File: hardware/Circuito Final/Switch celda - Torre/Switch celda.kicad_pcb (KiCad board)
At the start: 2 copper layers, 93.8 x 40 mm, 28 parts, among them Q1 MMBT2222A, Q2 MMBT2907A, Q3 MMBT2222A

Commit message: Subida de la versión torrecita
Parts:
- added TPgnd1: TP_gnd, Connector_PinHeader_2.54mm:PinHeader_1x01_P2.54mm_Vertical, F.Cu at (158.0, 111.2)
- added TPgnd2: TP_gnd, Connector_PinHeader_2.54mm:PinHeader_1x01_P2.54mm_Vertical, F.Cu at (151.0, 116.8)
- J_In_Out_1: value Conn_01x05_Socket -> Conn_01x06_Socket; footprint Connector_PinSocket_2.54mm:PinSocket_1x05_P2.54mm_Vertical -> Connector_PinSocket_2.54mm:PinSocket_1x06_P2.54mm_Vertical
- moved TP3 6.01 mm to (170.5, 115.5)
- moved TP1 4.75 mm to (165.8, 115.8)
- moved J_In_Out_1 2.54 mm to (103.5, 108.2)
- moved TP2 2.50 mm to (160.8, 115.8)
- moved Jumper_cell_neg_1 1.79 mm to (176.8, 116.8)
- moved Q3 0.59 mm to (151.2, 99.8), turned to 0 degrees
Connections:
- J_In_Out_1 pad 4: Vcc -> 0
- J_In_Out_1 pad 5: bus_pos -> Vcc
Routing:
- net Net-(Q2-B): track 37.5 -> 132.6 mm, vias 1 -> 0
- net Net-(Qinv1-D): track 53.3 -> 128.5 mm, vias 1 -> 0
- net bus_pos: track 14.9 -> 74.4 mm
- net 0: track 0.00 -> 9.42 mm
- net Net-(Q3-B): track 9.46 -> 4.79 mm
- net Net-(S1-G): track 155.5 -> 159.1 mm
- net Net-(Q3-C): track 10.0 -> 6.56 mm
- net Vcell_neg: track 108.8 -> 112.3 mm
- net bus_neg: track 65.6 -> 63.0 mm
- net cell_neg1: track 28.3 -> 26.5 mm
- net cell_neg4: track 17.6 -> 15.8 mm
- net cell_neg2: track 24.7 -> 23.0 mm
- net cell_neg6: track 10.4 -> 8.59 mm
- net cell_neg5: track 14.1 -> 12.3 mm
- net cell_neg3: track 21.2 -> 19.4 mm
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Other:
- board size 93.8 x 40 mm -> 97 x 40 mm

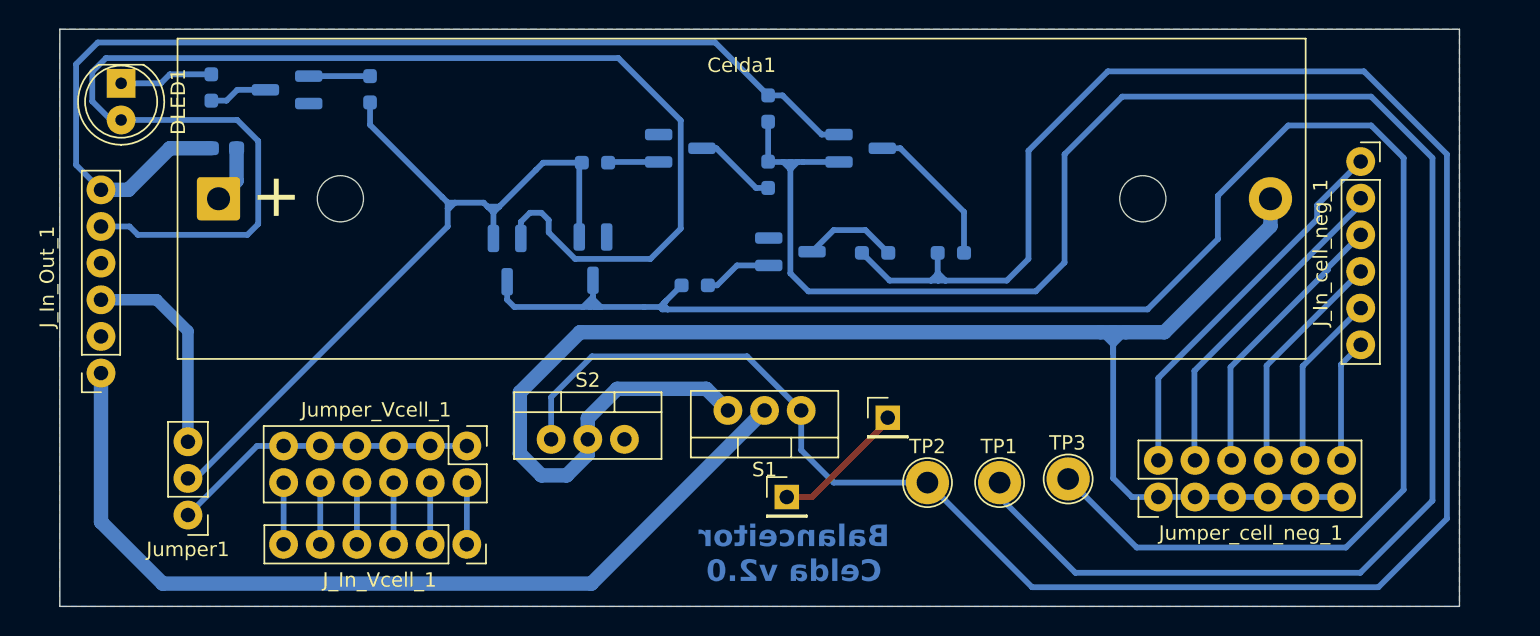
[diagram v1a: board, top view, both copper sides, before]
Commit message: Se duplican dos de las 3 tiras de pines del circuito de celda topología torre
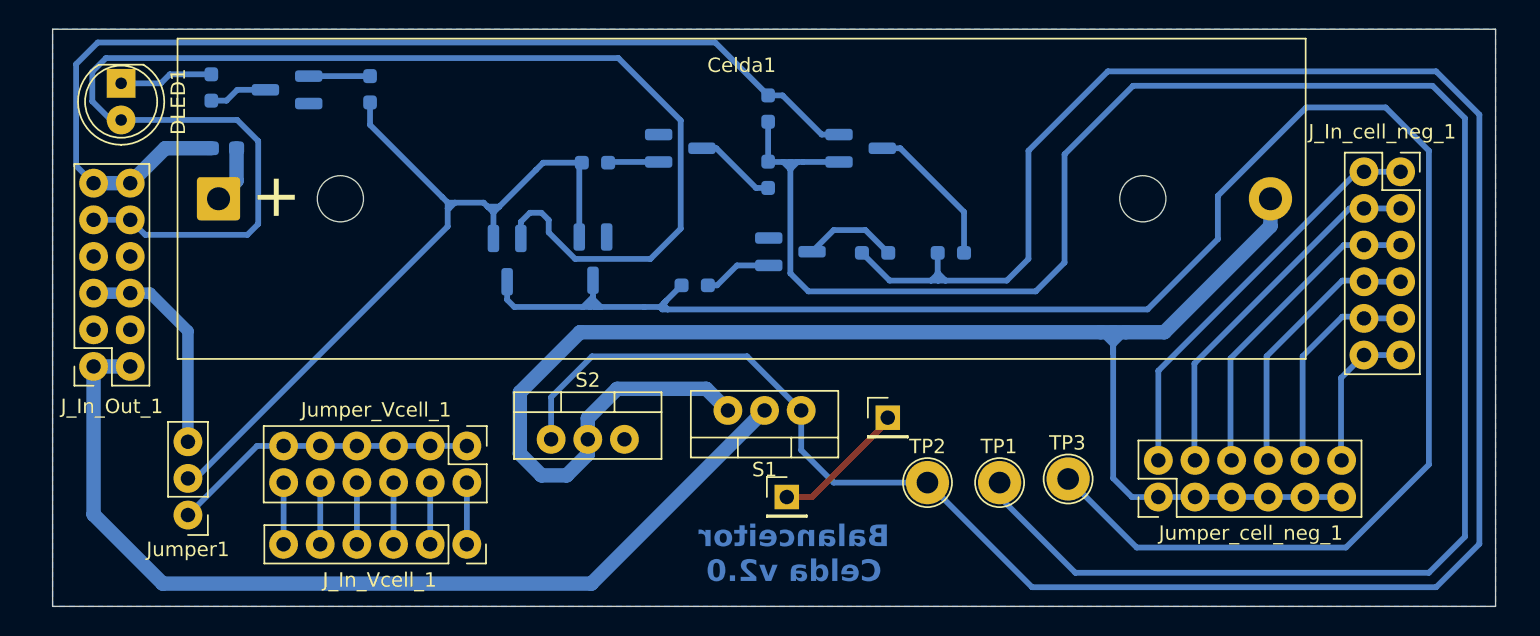
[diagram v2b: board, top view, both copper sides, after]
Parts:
- J_In_Out_1, J_In_cell_neg_1: value Conn_01x06_Socket -> Conn_02x06_Odd_Even; footprint Connector_PinSocket_2.54mm:PinSocket_1x06_P2.54mm_Vertical -> Connector_PinSocket_2.54mm:PinSocket_2x06_P2.54mm_Vertical
- moved J_In_cell_neg_1 2.85 mm to (193.5, 94.2)
- moved J_In_Out_1 0.69 mm to (103.0, 107.7)
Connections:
- J_In_Out_1 pad 2: 0 -> bus_neg
- J_In_Out_1 pad 3: Vcell_banco -> 0
- J_In_Out_1 pad 5: Vcc -> Vcell_banco
- J_In_Out_1 pad 6: bus_pos -> Vcell_banco
- J_In_cell_neg_1 pad 2: cell_neg2 -> cell_neg1
- J_In_cell_neg_1 pad 3: cell_neg3 -> cell_neg2
- J_In_cell_neg_1 pad 4: cell_neg4 -> cell_neg2
- J_In_cell_neg_1 pad 5: cell_neg5 -> cell_neg3
- J_In_cell_neg_1 pad 6: cell_neg6 -> cell_neg3
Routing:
- net Net-(Q2-B): track 132.6 -> 140.8 mm
- net Net-(S1-G): track 159.1 -> 166.3 mm
- net Net-(Qinv1-D): track 128.5 -> 132.3 mm
- net bus_neg: track 63.0 -> 66.3 mm
- net cell_neg5: track 12.3 -> 15.3 mm
- net cell_neg4: track 15.8 -> 18.8 mm
- net cell_neg3: track 19.4 -> 22.1 mm
- net cell_neg2: track 23.0 -> 25.5 mm
- net cell_neg1: track 26.5 -> 28.7 mm
- net cell_neg6: track 8.59 -> 10.5 mm
- net Vcc: track 97.5 -> 98.2 mm
- net Vcell_banco: track 14.6 -> 15.3 mm
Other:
- board size 97 x 40 mm -> 100 x 40 mm

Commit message: Cambios al circuito de la celda en modo torre: clearance de 0.5mm (en lugar de la mínima), buses de potencia de 1.5mm (en lugar de 1mm) y resistores SMD de tamaño 1206 (en lugar de 0603)
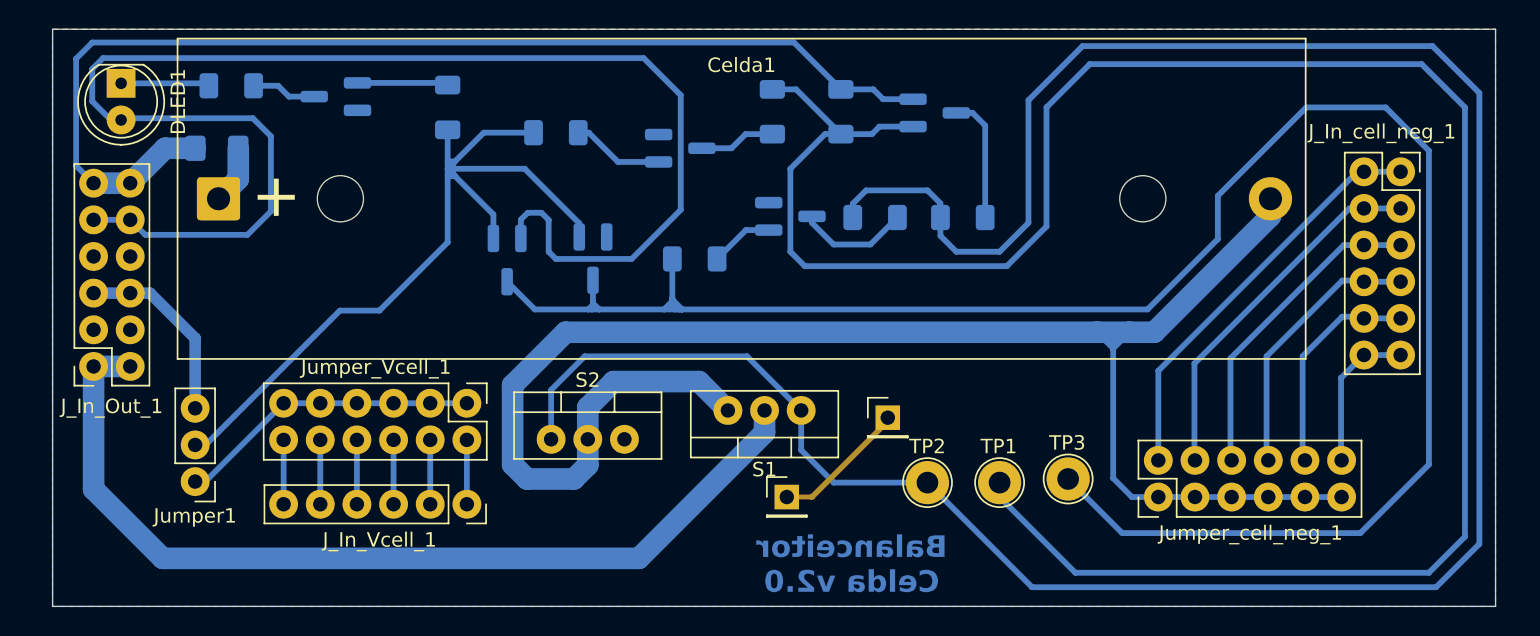
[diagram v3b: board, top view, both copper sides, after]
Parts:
- F1: footprint Fuse:Fuse_0603_1608Metric_Pad1.05x0.95mm_HandSolder -> Fuse:Fuse_1206_3216Metric_Pad1.42x1.75mm_HandSolder
- R1, R2, R3, R4, R5, R6, RLED1, RLED2: footprint Resistor_SMD:R_0603_1608Metric_Pad0.98x0.95mm_HandSolder -> Resistor_SMD:R_1206_3216Metric_Pad1.30x1.75mm_HandSolder
- moved Q2 5.69 mm to (161.2, 90.1)
- moved RLED1 5.53 mm to (127.5, 89.8)
- moved R2 5.05 mm to (154.8, 90.0)
- moved R3 4.38 mm to (150.0, 90.0)
- moved R1 3.41 mm to (135.0, 91.5)
- moved QLED1 3.41 mm to (119.8, 89.0)
- moved Jumper_Vcell_1 2.96 mm to (128.8, 110.2)
- moved J_In_Vcell_1 2.78 mm to (128.8, 117.2)
- moved R4 2.59 mm to (163.2, 97.4)
- moved Q3 2.45 mm to (151.2, 97.3)
- moved R5 2.45 mm to (157.1, 97.4)
- moved Jumper1 2.37 mm to (110.0, 115.7)
- moved R6 1.83 mm to (144.6, 100.2)
- moved RLED2 1.38 mm to (112.5, 88.2), turned to 180 degrees
- moved F1 0.50 mm to (111.5, 92.6)
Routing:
- net Net-(Q2-B): track 140.8 -> 146.7 mm
- net Vcell_neg: track 112.3 -> 116.0 mm
- net bus_pos: track 74.0 -> 77.7 mm
- net Net-(S1-G): track 166.3 -> 169.5 mm
- net Vin: track 55.6 -> 58.7 mm
- net Net-(Q1-B): track 3.52 -> 6.41 mm
- net Vcc: track 98.2 -> 101.0 mm
- net Vcell_banco: track 15.3 -> 13.2 mm
- net Net-(QLED1-B): track 4.25 -> 6.31 mm
- net Net-(Q2-C): track 10.3 -> 8.74 mm
- net bus_neg: track 66.3 -> 64.7 mm
- net Net-(Q3-C): track 6.56 -> 7.77 mm
- net Net-(Qinv1-D): track 132.3 -> 133.3 mm

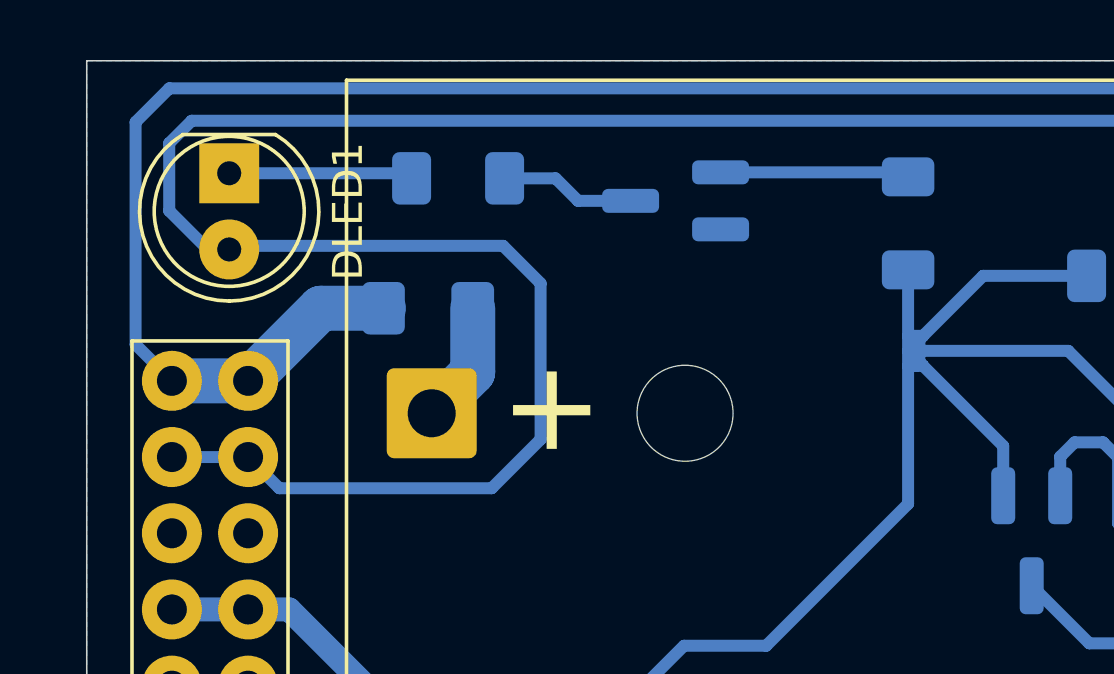
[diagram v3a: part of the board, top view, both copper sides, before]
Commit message: Update menor de orden de señales en la entrada (VCC por bus_pos)
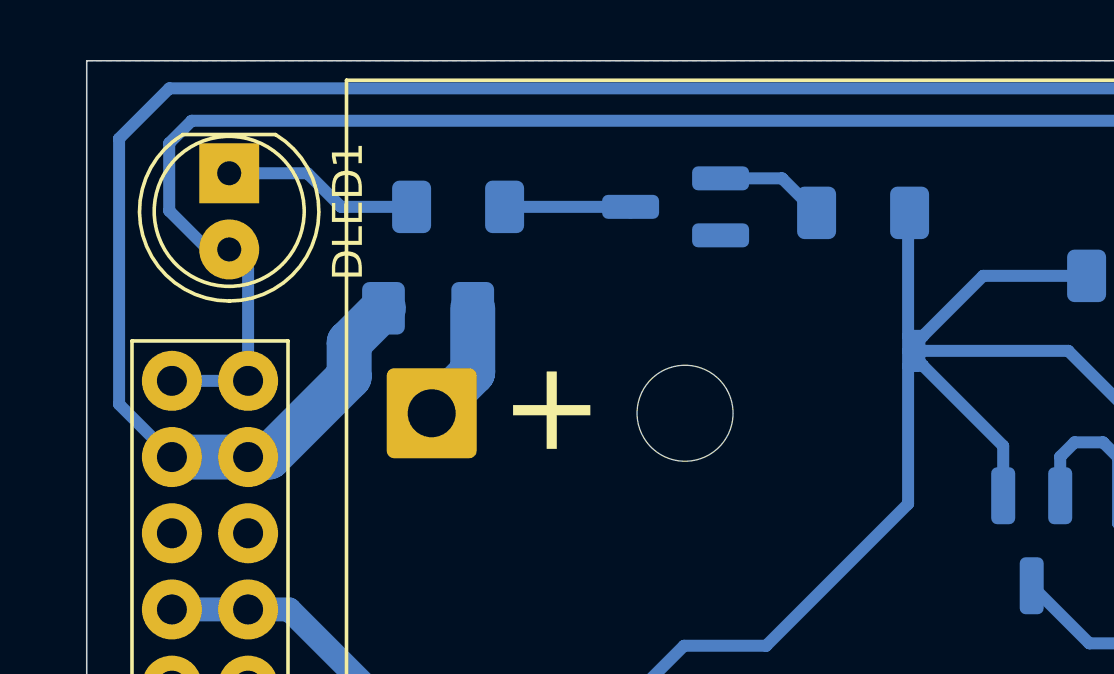
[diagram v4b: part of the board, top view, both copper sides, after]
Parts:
- moved RLED1 1.54 mm to (126.0, 89.4), turned to 180 degrees
- moved RLED2 0.95 mm to (112.5, 89.2)
- moved QLED1 0.20 mm to (119.8, 89.2)
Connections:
- J_In_Out_1 pad 10: Vcc -> bus_pos
- J_In_Out_1 pad 11: bus_pos -> Vcc
- J_In_Out_1 pad 12: bus_pos -> Vcc
- J_In_Out_1 pad 9: Vcc -> bus_pos
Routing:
- net Vcc: track 101.0 -> 78.7 mm
- net bus_pos: track 77.7 -> 82.4 mm
- net Net-(QLED1-B): track 6.31 -> 3.68 mm
- net Vin: track 58.7 -> 60.9 mm

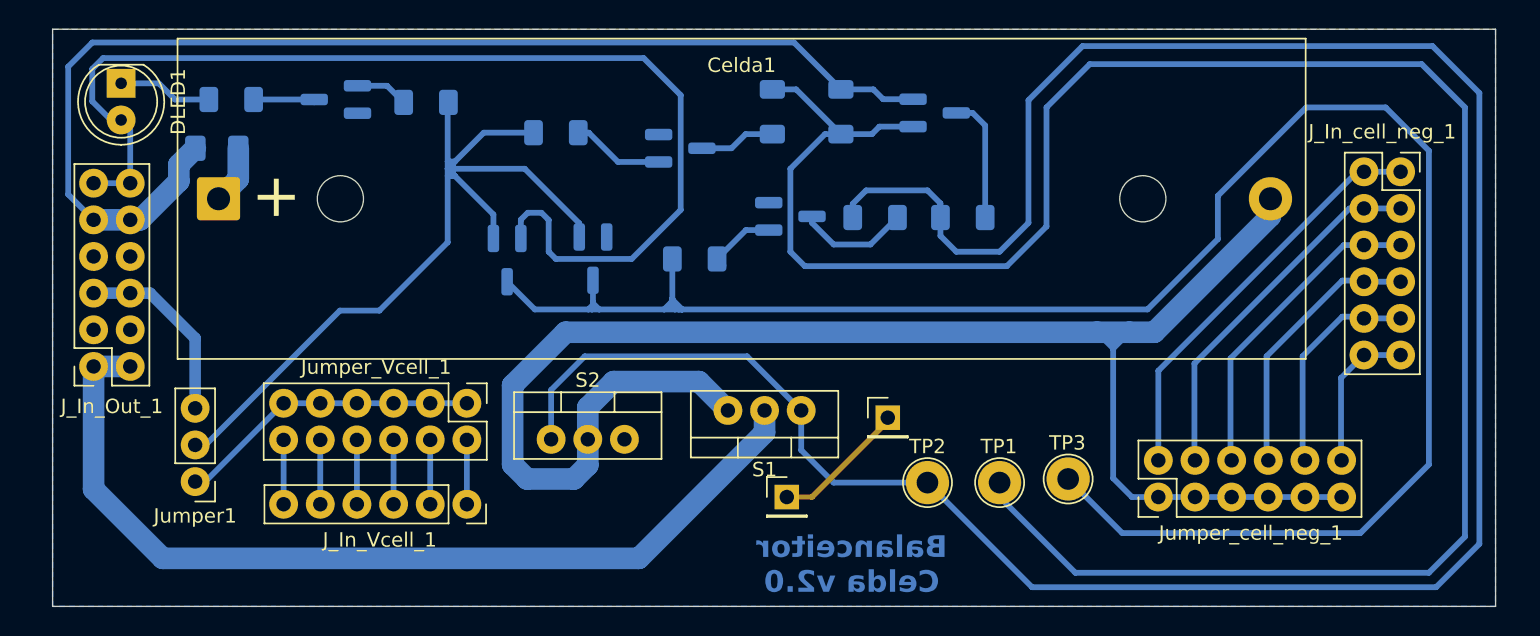
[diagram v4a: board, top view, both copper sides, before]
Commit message: Update switch celda: ahora tiene pines para conectarse con 7 celdas en lugar de 6
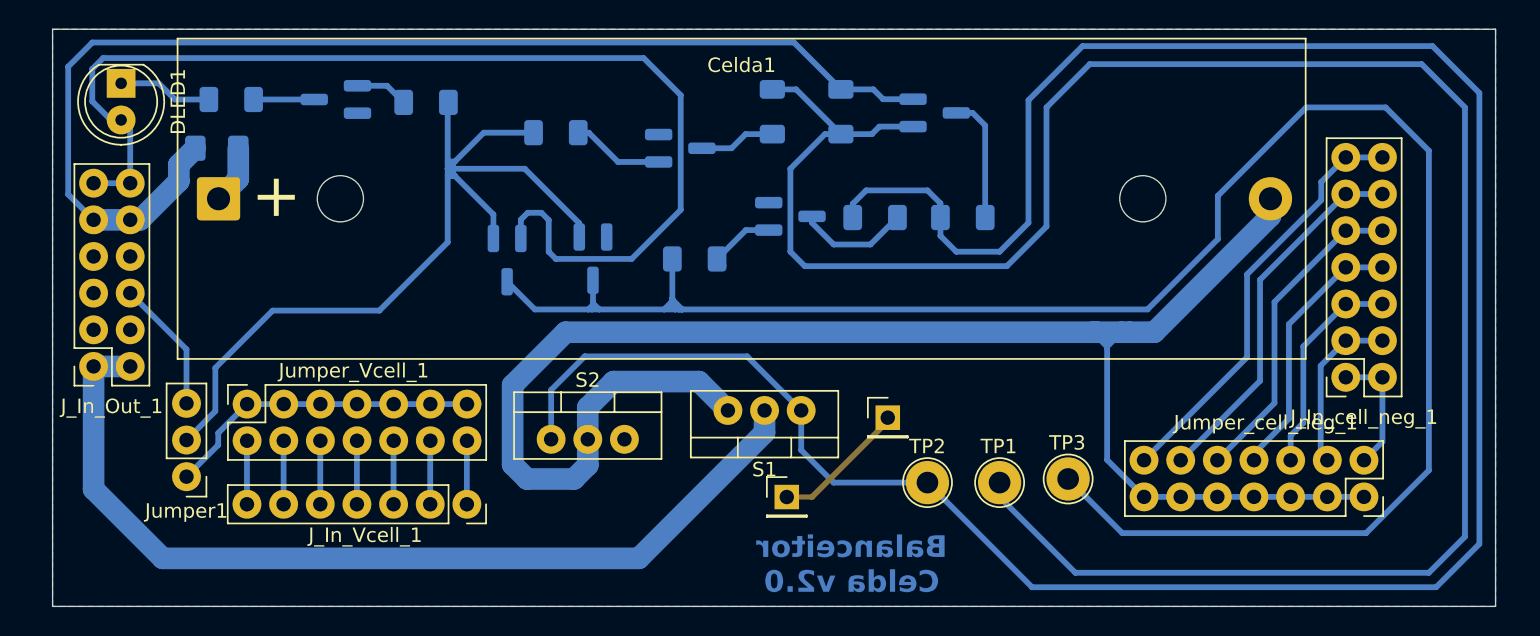
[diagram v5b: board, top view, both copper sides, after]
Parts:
- J_In_Vcell_1: value Conn_01x06_Socket -> Conn_01x07_Socket; footprint Connector_PinSocket_2.54mm:PinSocket_1x06_P2.54mm_Vertical -> Connector_PinSocket_2.54mm:PinSocket_1x07_P2.54mm_Vertical
- J_In_cell_neg_1: value Conn_02x06_Odd_Even -> Conn_02x07_Odd_Even; footprint Connector_PinSocket_2.54mm:PinSocket_2x06_P2.54mm_Vertical -> Connector_PinSocket_2.54mm:PinSocket_2x07_P2.54mm_Vertical
- Jumper_Vcell_1, Jumper_cell_neg_1: value Conn_02x06_Odd_Even -> Conn_02x07_Odd_Even; footprint Connector_PinHeader_2.54mm:PinHeader_2x06_P2.54mm_Vertical -> Connector_PinSocket_2.54mm:PinSocket_2x07_P2.54mm_Vertical
- moved Jumper_Vcell_1 15.2 mm to (113.6, 110.3), turned to 90 degrees
- moved J_In_cell_neg_1 14.7 mm to (189.7, 108.5), turned to 180 degrees
- moved Jumper_cell_neg_1 14.3 mm to (191.0, 116.7), turned to -90 degrees
- moved Jumper1 0.69 mm to (109.4, 115.3)
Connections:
- Jumper_Vcell_1 pad 10: Vcell5 -> Vcell3
- Jumper_Vcell_1 pad 12: Vcell6 -> Vcell2
- Jumper_Vcell_1 pad 2: Vcell1 -> Vcell7
- Jumper_Vcell_1 pad 4: Vcell2 -> Vcell6
- Jumper_Vcell_1 pad 6: Vcell3 -> Vcell5
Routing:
- net cell_neg7: track 0.00 -> 29.3 mm
- net cell_neg1: track 28.7 -> 8.82 mm
- net cell_neg6: track 10.5 -> 25.7 mm
- net cell_neg2: track 25.5 -> 11.7 mm
- net cell_neg3: track 22.1 -> 15.0 mm
- net cell_neg5: track 15.3 -> 22.1 mm
- net Vcell7: track 0.00 -> 4.41 mm
- net Vcell_banco: track 13.2 -> 9.26 mm
- net Vin: track 60.9 -> 63.1 mm
- net Vcell: track 21.1 -> 22.0 mm

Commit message: Subida de datasheets y corrección de uno de los pines de entradas
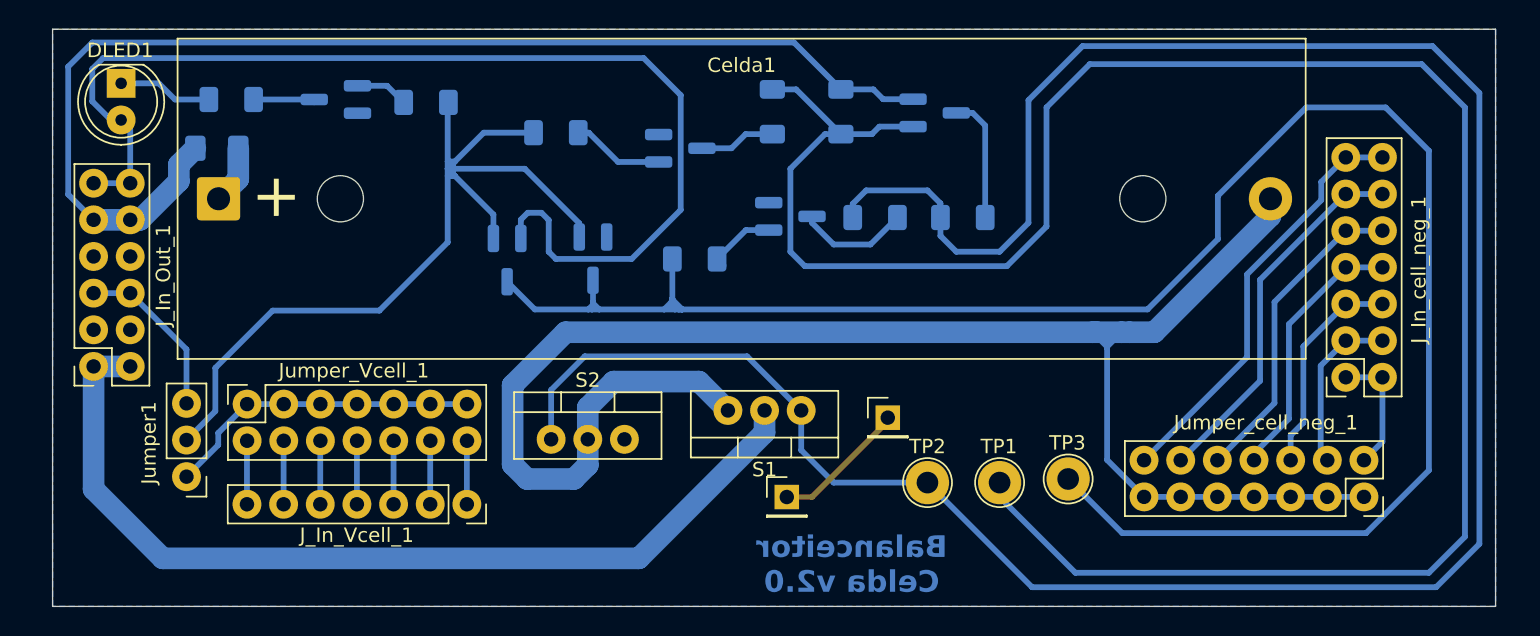
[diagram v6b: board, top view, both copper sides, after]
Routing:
- net Vcell_banco: track 9.26 -> 11.8 mm
